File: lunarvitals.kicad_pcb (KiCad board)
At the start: 2 copper layers, 40 x 36 mm, 28 parts, among them J1 MLX90614, J2 MAX30102, J3 SEN11574, J4 ConductiveCord, U1 NRF52840-DONGLE, U2 BMP280, U3 AP2112K-3.3, U5 MPU-6050

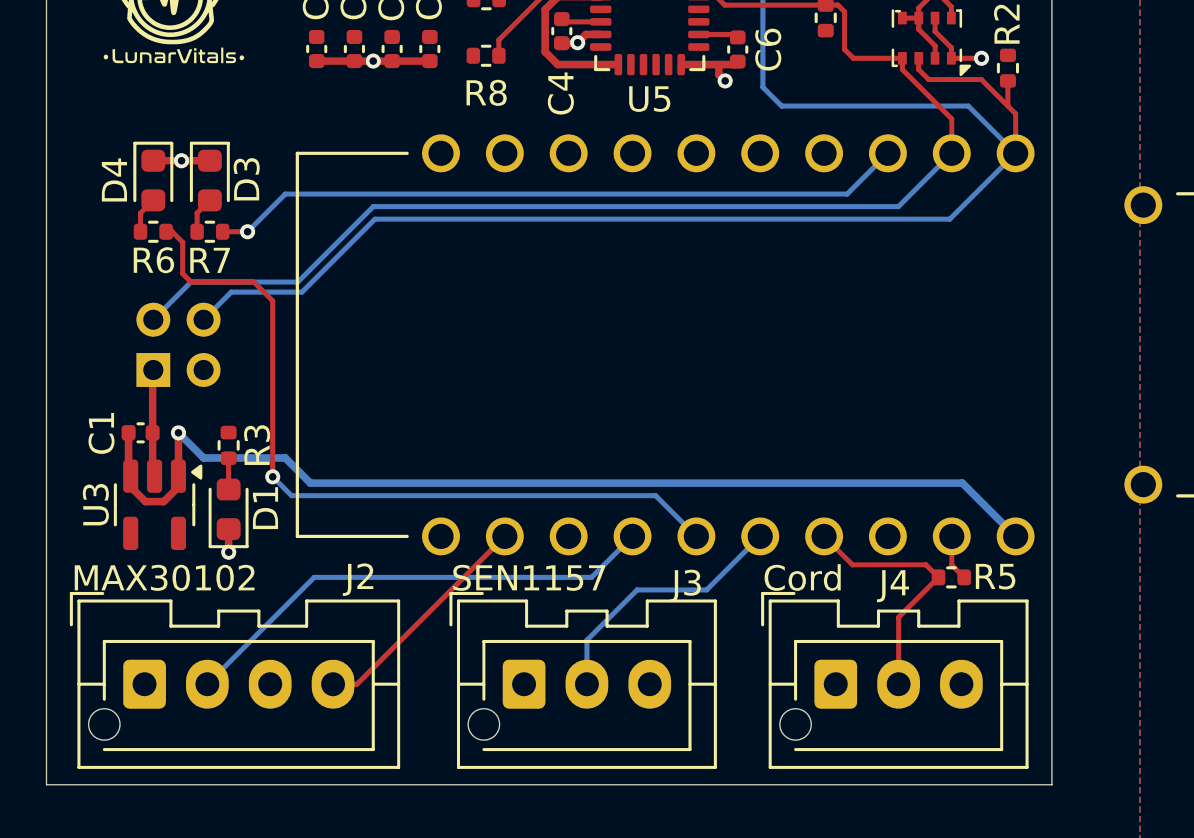
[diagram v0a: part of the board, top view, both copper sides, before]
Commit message: removed 2 voltage regulator on same 3.3v connection
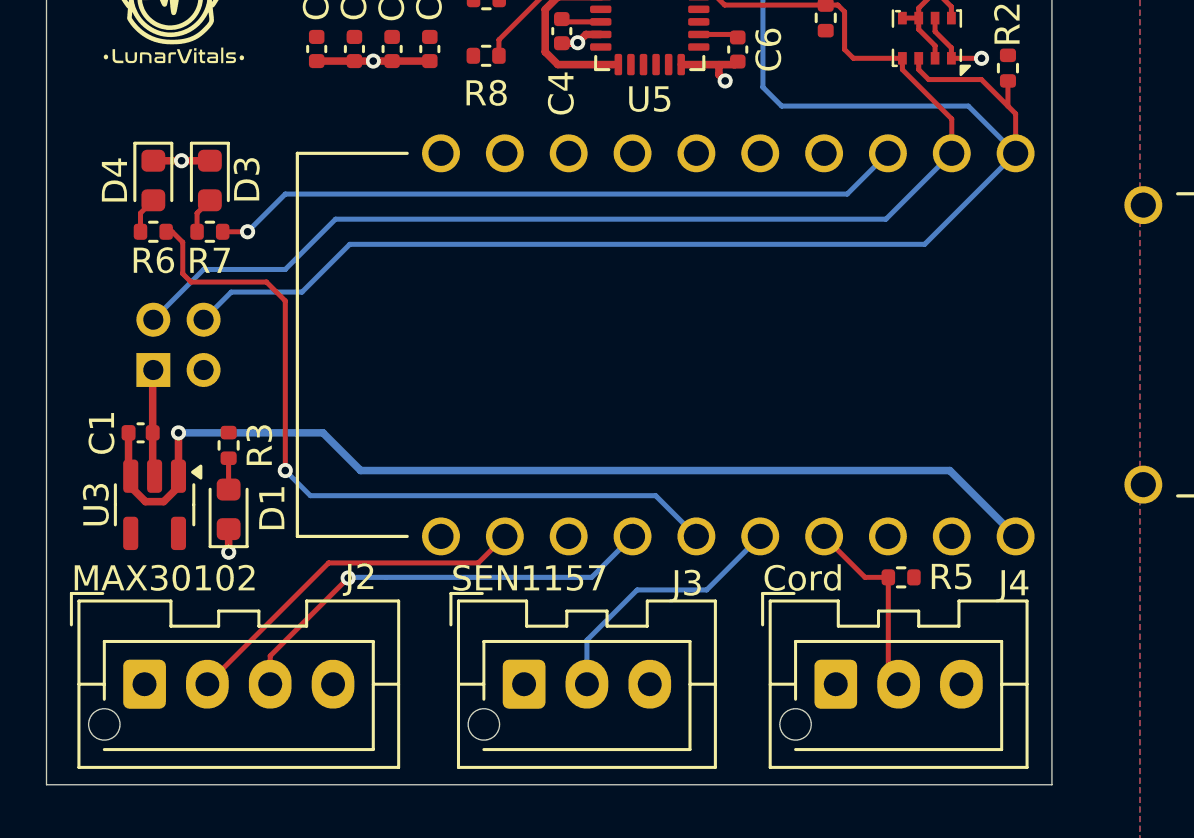
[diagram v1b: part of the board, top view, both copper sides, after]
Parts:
- moved R5 2.00 mm to (183.5, 119.2)
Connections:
- J2 pad 1: GND -> +3.3V
- J2 pad 2: /I2C1_SCL -> /I2C1_SDA
- J2 pad 3: +3.3V -> /I2C1_SCL
- J2 pad 4: /I2C1_SDA -> GND
- U1 pad OUT: +3.3V -> unconnected-(U1-PadOUT)
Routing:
- net /I2C1_SDA: track 9.27 -> 14.3 mm
- net /AIN7: track 10.1 -> 7.65 mm
- net +3.3V: track 14.8 -> 12.4 mm
- net /I2C1_SCL: track 19.4 -> 17.5 mm, vias 0 -> 1

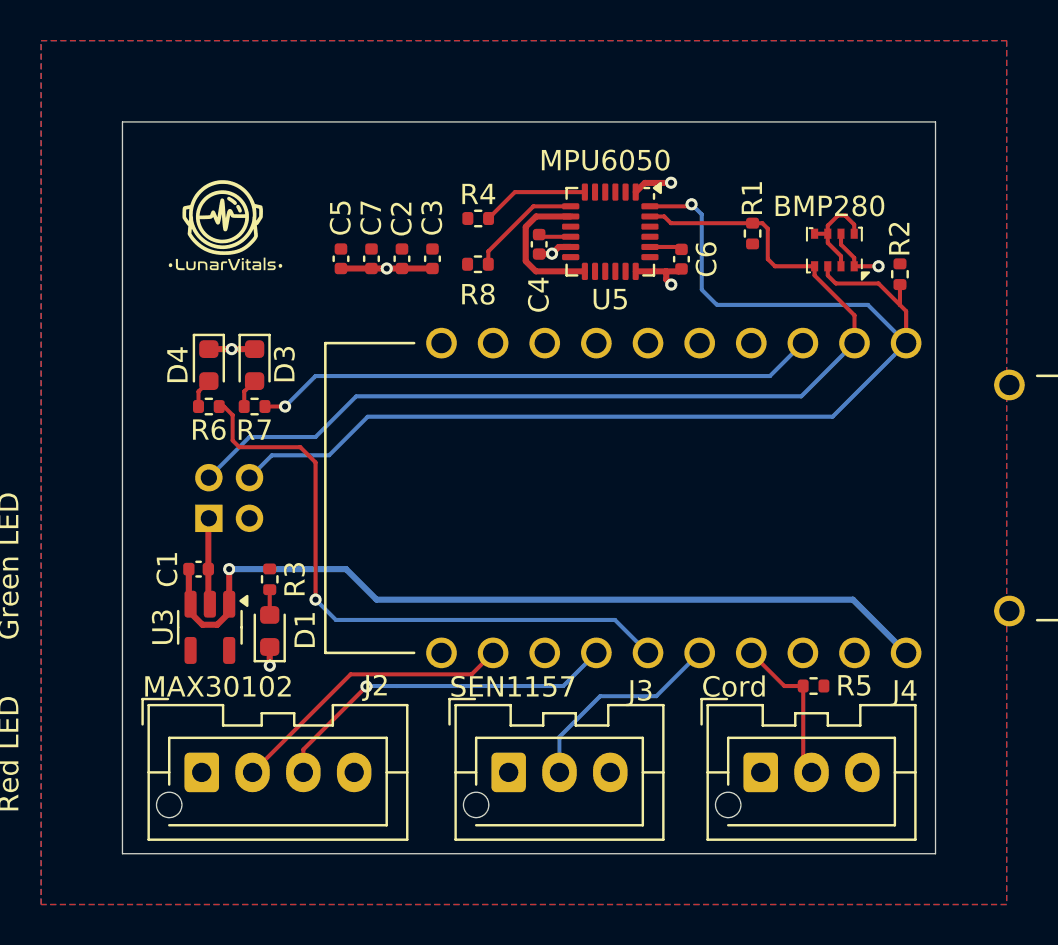
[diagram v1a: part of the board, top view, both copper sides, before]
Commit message: fix capacitor positioning
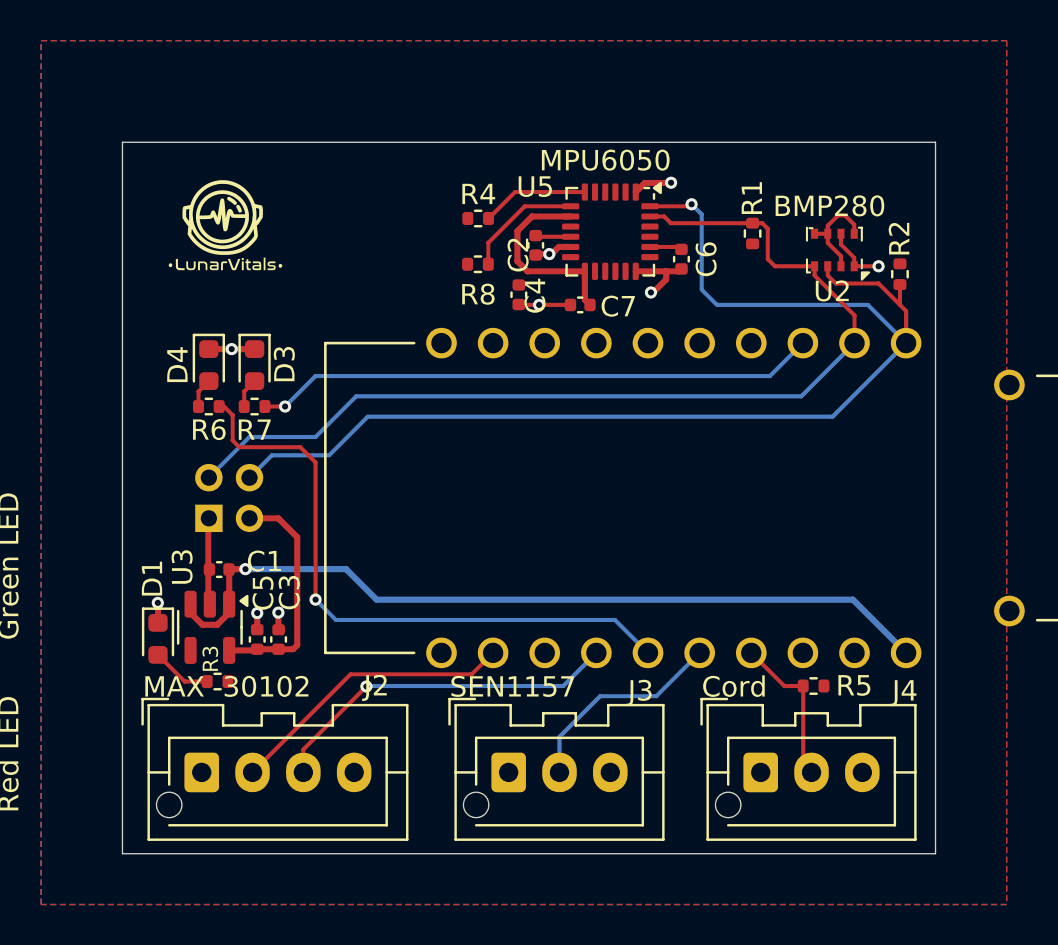
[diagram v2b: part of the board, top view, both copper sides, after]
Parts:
- moved C3 20.2 mm to (157.2, 117.0), turned to 90 degrees
- moved C5 19.2 mm to (156.1, 117.0), turned to 90 degrees
- moved C7 10.5 mm to (172.0, 100.5), turned to 180 degrees
- moved C2 6.02 mm to (169.0, 100.0)
- moved R3 5.65 mm to (154.2, 119.0), turned to 180 degrees
- moved D1 5.51 mm to (151.2, 116.9), turned to -90 degrees
- moved C1 1.02 mm to (154.3, 113.5), turned to 180 degrees
- moved C4 0.18 mm to (169.8, 97.6)
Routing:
- net +3.3V: track 12.4 -> 26.6 mm
- net Net-(D1-A): track 1.24 -> 2.96 mm
- net +5V: track 41.7 -> 40.1 mm
- net GND: track 21.7 -> 22.2 mm, vias 7 -> 9
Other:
- board size 40 x 36 mm -> 40 x 35 mm
- board text added: "MAX 30102"
- board text removed: "MAX30102"

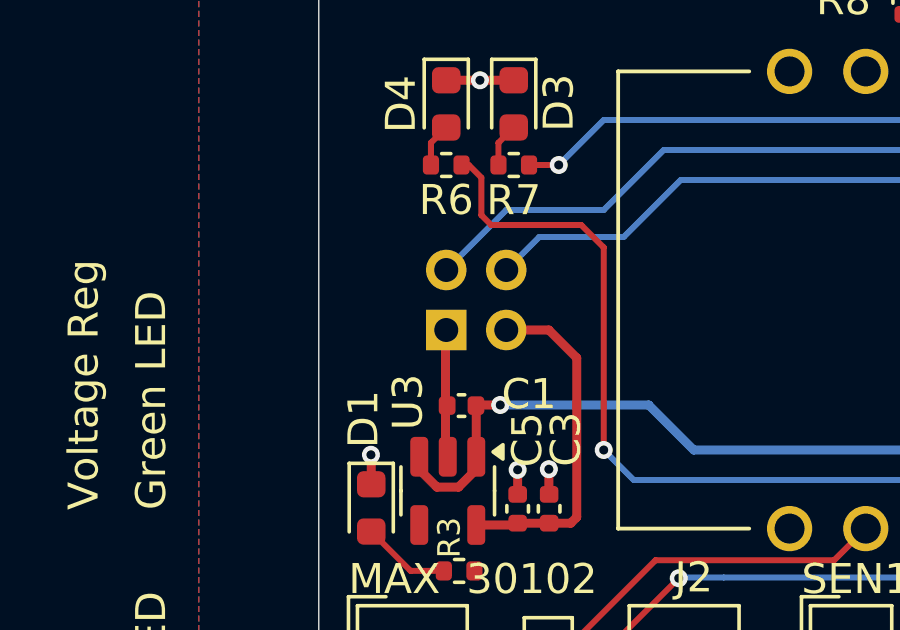
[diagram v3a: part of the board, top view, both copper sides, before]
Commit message: add keepout for dongle antenna
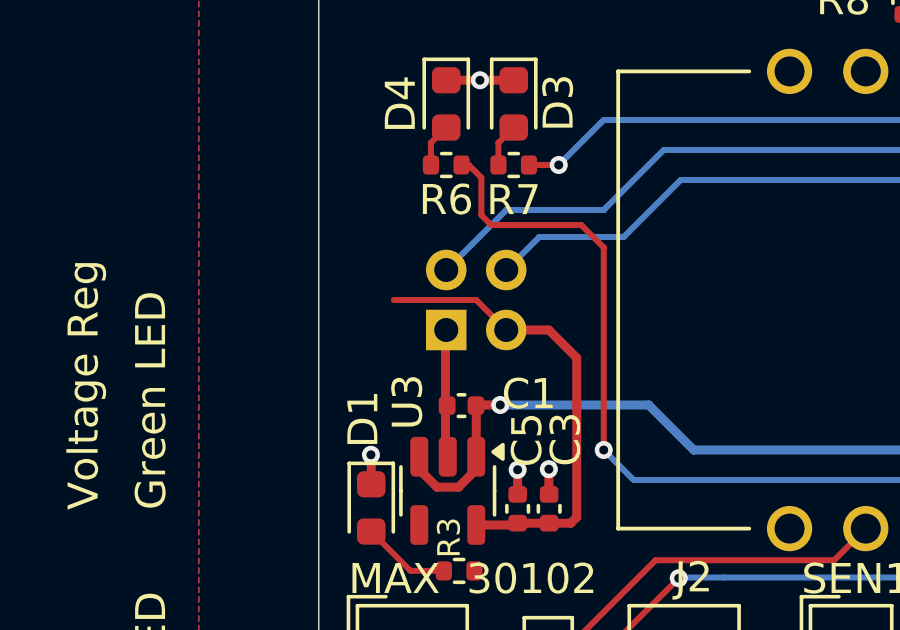
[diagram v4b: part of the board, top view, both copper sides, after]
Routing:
- net +3.3V: track 26.6 -> 30.8 mm
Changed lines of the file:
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@@
+	)
+	(segment
+		(start 155.75 111)
+		(end 154.75 110)
+		(width 0.2)
+		(layer "F.Cu")
+		(net 5)
 	)
 	(segment
@@
 		(end 157.18 117.44)
 		(width 0.3)
+		(layer "F.Cu")
+		(net 5)
+	)
+	(segment
+		(start 154.75 110)
+		(end 152 110)
+		(width 0.2)
 		(layer "F.Cu")
 		(net 5)
@@
 			)
 		)
+	)
+	(zone
+		(net 0)
+		(net_name "")
+		(layers "F&B.Cu")
+		(hatch edge 0.5)
+		(connect_pads
+			(clearance 0)
+		)
+		(min_thickness 0.25)
+		(filled_areas_thickness no)
+		(keepout
+			(tracks allowed)
+			(vias allowed)
+			(pads allowed)
+			(copperpour not_allowed)
+			(footprints allowed)
+		)
+		(fill
+			(thermal_gap 0.5)
+			(thermal_bridge_width 0.5)
+		)
+		(polygon
+			(pts
+				(xy 166 100) (xy 166 120) (xy 158.5 120) (xy 158.5 100)
+			)
+		)

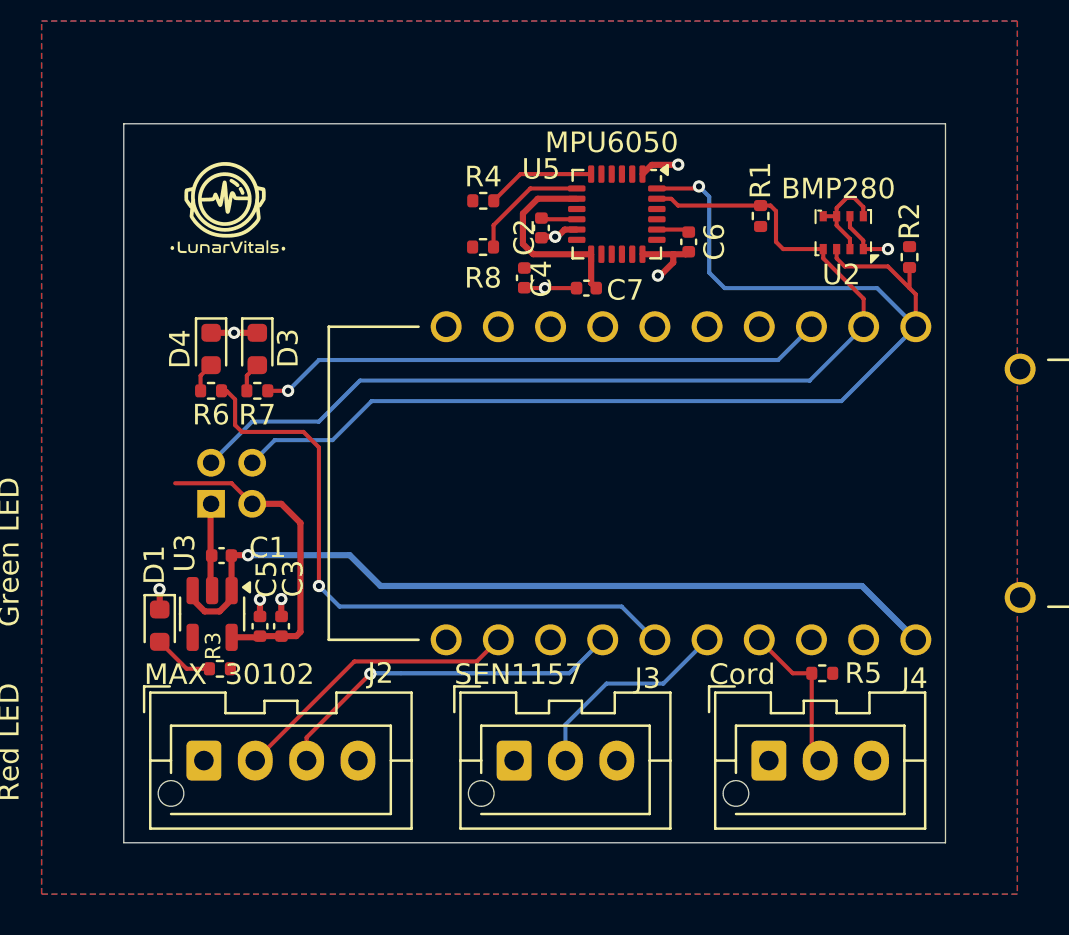
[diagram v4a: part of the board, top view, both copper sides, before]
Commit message: add scuffed mounting holes (better than none)
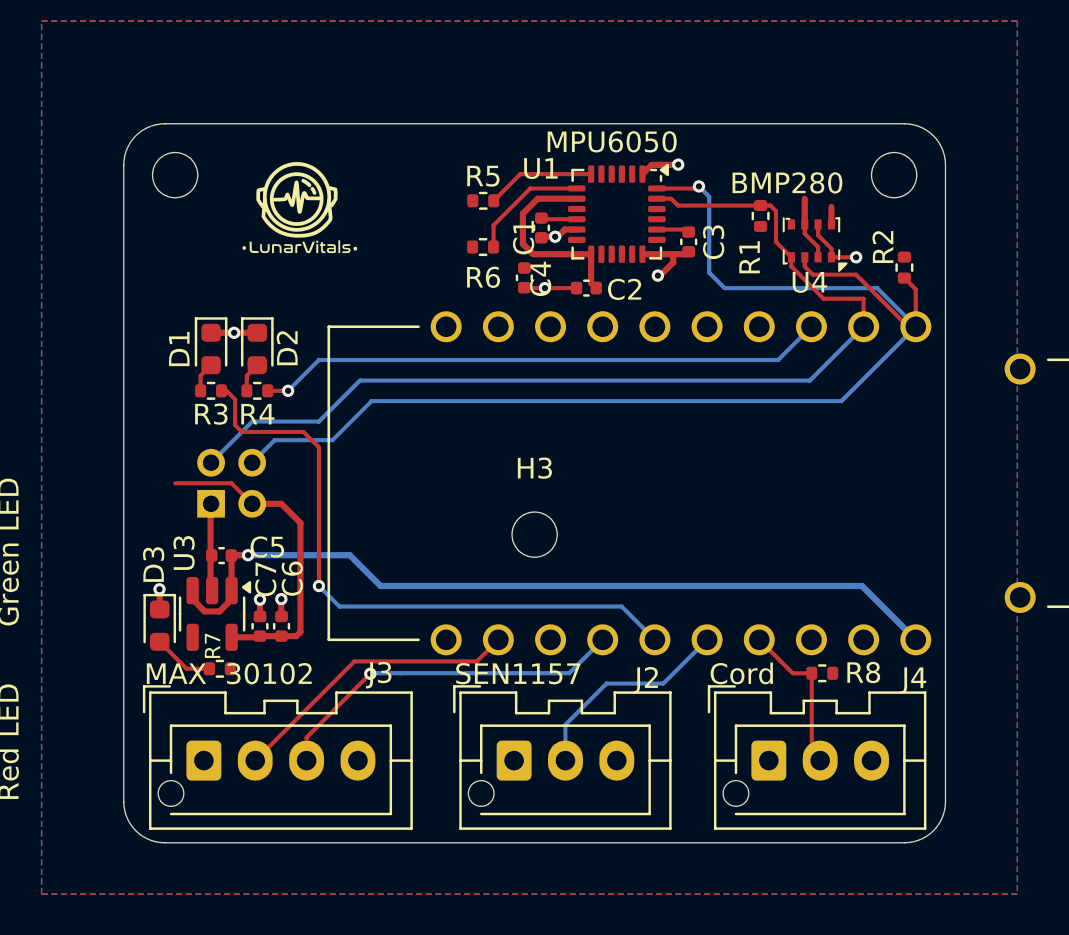
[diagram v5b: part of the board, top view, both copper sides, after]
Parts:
- added H1: MountingHole, MountingHole:MountingHole_2.2mm_M2, F.Cu at (152.0, 95.0)
- added H2: MountingHole, MountingHole:MountingHole_2.2mm_M2, F.Cu at (187.0, 95.0)
- added H3: MountingHole, MountingHole:MountingHole_2.2mm_M2, F.Cu at (169.5, 112.5)
- moved G*** 3.50 mm to (158.0, 96.5)
- moved U4 1.60 mm to (183.0, 98.2)
- moved R2 0.57 mm to (187.5, 99.5)
- renumbered C2 to C1, C7 to C2, C6 to C3, C1 to C5, C3 to C6, C5 to C7, D4 to D1, D3 to D2, D1 to D3, J3 to J2, J2 to J3, R6 to R3, R7 to R4, R4 to R5, R8 to R6, R3 to R7, R5 to R8, U5 to U1, U1 to U2, U2 to U4
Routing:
- net /I2C0_SDA: track 60.3 -> 62.4 mm
- net +3.3V: track 30.8 -> 29.7 mm
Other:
- outline, holes or cut-outs redrawn

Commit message: PCB Updates
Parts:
- removed C7: 0.1uf, Capacitor_SMD:C_0402_1005Metric
- removed the G*** at (158.0, 96.5)
- removed J4: ConductiveCord, Connector_JST:JST_XA_B03B-XASK-1-A_1x03_P2.50mm_Vertical
- removed the R3 at (153.8, 105.5)
- removed the R5 at (167.0, 96.2)
- removed the U1 at (173.5, 96.9)
- added D2: Red_LED, LED_SMD:LED_0603_1608Metric, F.Cu at (149.2, 121.0)
- added D5: Blue_LED, LED_SMD:LED_0603_1608Metric, F.Cu at (149.2, 119.0)
- added G***: LOGO, lunar_vitals_custom:lunarvitals_logo_big, F.Cu at (173.0, 96.5)
- added J5: USB_C_Receptacle_PowerOnly_6P, Connector_USB:USB_C_Receptacle_GCT_USB4125-xx-x-0190_6P_TopMnt_Horizontal, F.Cu at (142.3, 110.0)
- added J6: Battery, SM02B-SRSS-TB_LF__SN_:SM02B-SRSS-TB_LF__SN_, F.Cu at (152.2, 95.9)
- added Q1: FS8205A, FS8205A:SOP65P640X120-8N, F.Cu at (142.5, 100.0)
- added R10: 1k, Resistor_SMD:R_0402_1005Metric, F.Cu at (149.5, 123.0)
- added R11: 1k, Resistor_SMD:R_0402_1005Metric, F.Cu at (148.0, 123.0)
- added R12: 100, Resistor_SMD:R_0402_1005Metric, F.Cu at (145.0, 99.5)
- added R13: 1k, Resistor_SMD:R_0402_1005Metric, F.Cu at (152.0, 100.0)
- added R7: 5.1k, Resistor_SMD:R_0402_1005Metric, F.Cu at (147.5, 109.0)
- added R8: 5.1k, Resistor_SMD:R_0402_1005Metric, F.Cu at (147.5, 111.0)
- added R9: 2.4k, Resistor_SMD:R_0402_1005Metric, F.Cu at (145.5, 116.0)
- added U4: TP4056, TP4056:SOP127P600X175-9N, F.Cu at (144.4, 120.3)
- added U5: MLX90614ESF-AAA-000-TU, MLX90614ESF-AAA-000-TU:TO254P912H435-4, B.Cu at (153.5, 110.0)
- added U6: DW01A, Package_TO_SOT_SMD:SOT-23-6, F.Cu at (148.9, 100.0)
- C1: value 10nf -> 4.7uf
- C2: value 0.1uf -> 10uf
- C3: value 2.2nf -> 0.1uf
- C5: value 4.7uf -> 0.1uf
- J1: value MLX90614 -> ConductiveCord; footprint Connector_PinSocket_2.00mm:PinSocket_2x02_P2.00mm_Vertical -> Connector_JST:JST_XH_B2B-XH-AM_1x02_P2.50mm_Vertical; moved to F.Cu
- J2: renamed from J3; value MAX30102 -> MPU6050; footprint Connector_JST:JST_XA_B04B-XASK-1-A_1x04_P2.50mm_Vertical -> Connector_JST:JST_XH_B4B-XH-AM_1x04_P2.50mm_Vertical
- J3: renamed from J2; footprint Connector_JST:JST_XA_B03B-XASK-1-A_1x03_P2.50mm_Vertical -> Connector_JST:JST_XH_B3B-XH-AM_1x03_P2.50mm_Vertical
- R6: value 4.7k -> 330
- moved J1 31.6 mm to (183.0, 123.0), turned to 0 degrees
- moved C3 27.8 mm to (156.0, 116.5), turned to 90 degrees
- moved C4 27.1 mm to (147.5, 113.0), turned to 90 degrees
- moved C2 21.9 mm to (157.0, 116.5), turned to 90 degrees
- moved H3 20.4 mm to (153.0, 124.5)
- moved C1 19.5 mm to (156.5, 115.0), turned to 0 degrees
- moved C6 16.9 mm to (141.1, 122.3)
- moved C5 15.4 mm to (146.0, 100.5), turned to -90 degrees
- moved R6 10.7 mm to (157.5, 103.5), turned to -90 degrees
- moved H1 7.00 mm to (159.0, 95.0)
- moved J2 5.12 mm to (158.5, 123.0)
- moved J3 3.54 mm to (172.0, 123.0)
- moved D1 3.44 mm to (154.0, 119.0), turned to 0 degrees
- moved D4 2.68 mm to (155.5, 105.5), turned to 0 degrees
- moved R3 1.50 mm to (154.5, 120.5), turned to 0 degrees
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- renumbered D3 to D1, D2 to D3, D1 to D4, R7 to R3, R8 to R5, U2 to U1, U4 to U2
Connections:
- C1 pad 1: +3.3V -> BOut+
- C3 pad 1: Net-(U1-CPOUT) -> +3.3V
- C4 pad 1: Net-(U1-REGOUT) -> +5V
- C5 pad 1: +5V -> Net-(U6-VCC)
- C5 pad 2: GND -> /B-
- C6 pad 1: +3.3V -> BOut+
- D3 pad 2: Net-(D2-A) -> Net-(D3-A)
- D4 pad 2: Net-(D1-A) (its old number) -> Net-(D4-A)
- J1 pad 1: GND -> /AIN7
- J1 pad 2: /I2C0_SCL -> +3.3V
- J2 pad 2: /I2C1_SDA -> GND
- J2 pad 3: /I2C1_SCL -> /I2C1_SDA
- J2 pad 4: GND -> /I2C1_SCL
- R4 pad 1: /GPIO17 -> /GPIO2
- R4 pad 2: Net-(D2-A) -> Net-(D4-A)
- R6 pad 1: +3.3V -> /GPIO17
- R6 pad 2: Net-(U1-AUX_CL) -> Net-(D3-A)
- U1 pad OUT: unconnected-(U2-PadOUT) -> +3.3V
- U1 pad VBUS: +5V -> unconnected-(U1-PadVBUS)
- U3 pad 1: +5V -> BOut+
- U3 pad 3: +5V -> BOut+
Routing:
- net BOut+: track 0.00 -> 53.3 mm, vias 0 -> 3
- net GND: track 22.2 -> 46.1 mm, vias 9 -> 5
- net +3.3V: track 29.7 -> 7.02 mm
- net /B-: track 0.00 -> 13.1 mm
- net +5V: track 40.1 -> 29.1 mm, vias 1 -> 2
- net Net-(U6-OC): track 0.00 -> 10.1 mm, vias 0 -> 2
- net /I2C0_SDA: track 62.4 -> 52.5 mm, vias 1 -> 0
- net /I2C1_SCL: track 17.5 -> 9.92 mm, vias 1 -> 0
- net Net-(U4-~{STDBY}): track 0.00 -> 7.39 mm
- net Net-(U6-OD): track 0.00 -> 7.32 mm
- net /I2C1_SDA: track 14.3 -> 7.13 mm
- net Net-(U1-AUX_CL): track 5.85 -> 0.00 mm
- net /I2C0_SCL: track 49.2 -> 54.7 mm
- net Net-(U1-AUX_DA): track 5.28 -> 0.00 mm
- net Net-(U4-~{CHRG}): track 0.00 -> 4.30 mm
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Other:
- board size 40 x 35 mm -> 49.5 x 35 mm
- board text added: "MPU 6050"
- board text removed: "Green LED"
- board text removed: "MAX 30102"
- board text removed: "MPU6050"
- board text removed: "Red LED"
- board text removed: "Voltage Reg"
